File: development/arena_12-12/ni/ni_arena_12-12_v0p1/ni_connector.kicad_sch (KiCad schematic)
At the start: 29 parts, among them J2 NI_TE_68pos

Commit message: Worked on fabrication setup for NI 12-12 arena.
Added part numbers, datasheets, etc. to symbol table.
Deleted old productions files.
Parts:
- J2: Digikey PN (none) -> A123166-ND; LCSC Part # (none) -> TODO; MPN (none) -> 5174339-5
- R1, R10, R11, R12, R13, R14, R15, R16, R17, R18, R19, R2, R20, R21, R22, R23, R24, R25, R26, R27, R28, R3, R4, R5, R6, R7, R8, R9: Digikey PN (none) -> (none); LCSC Part # (none) -> C25105; MPN (none) -> 0402WGF330JTCE

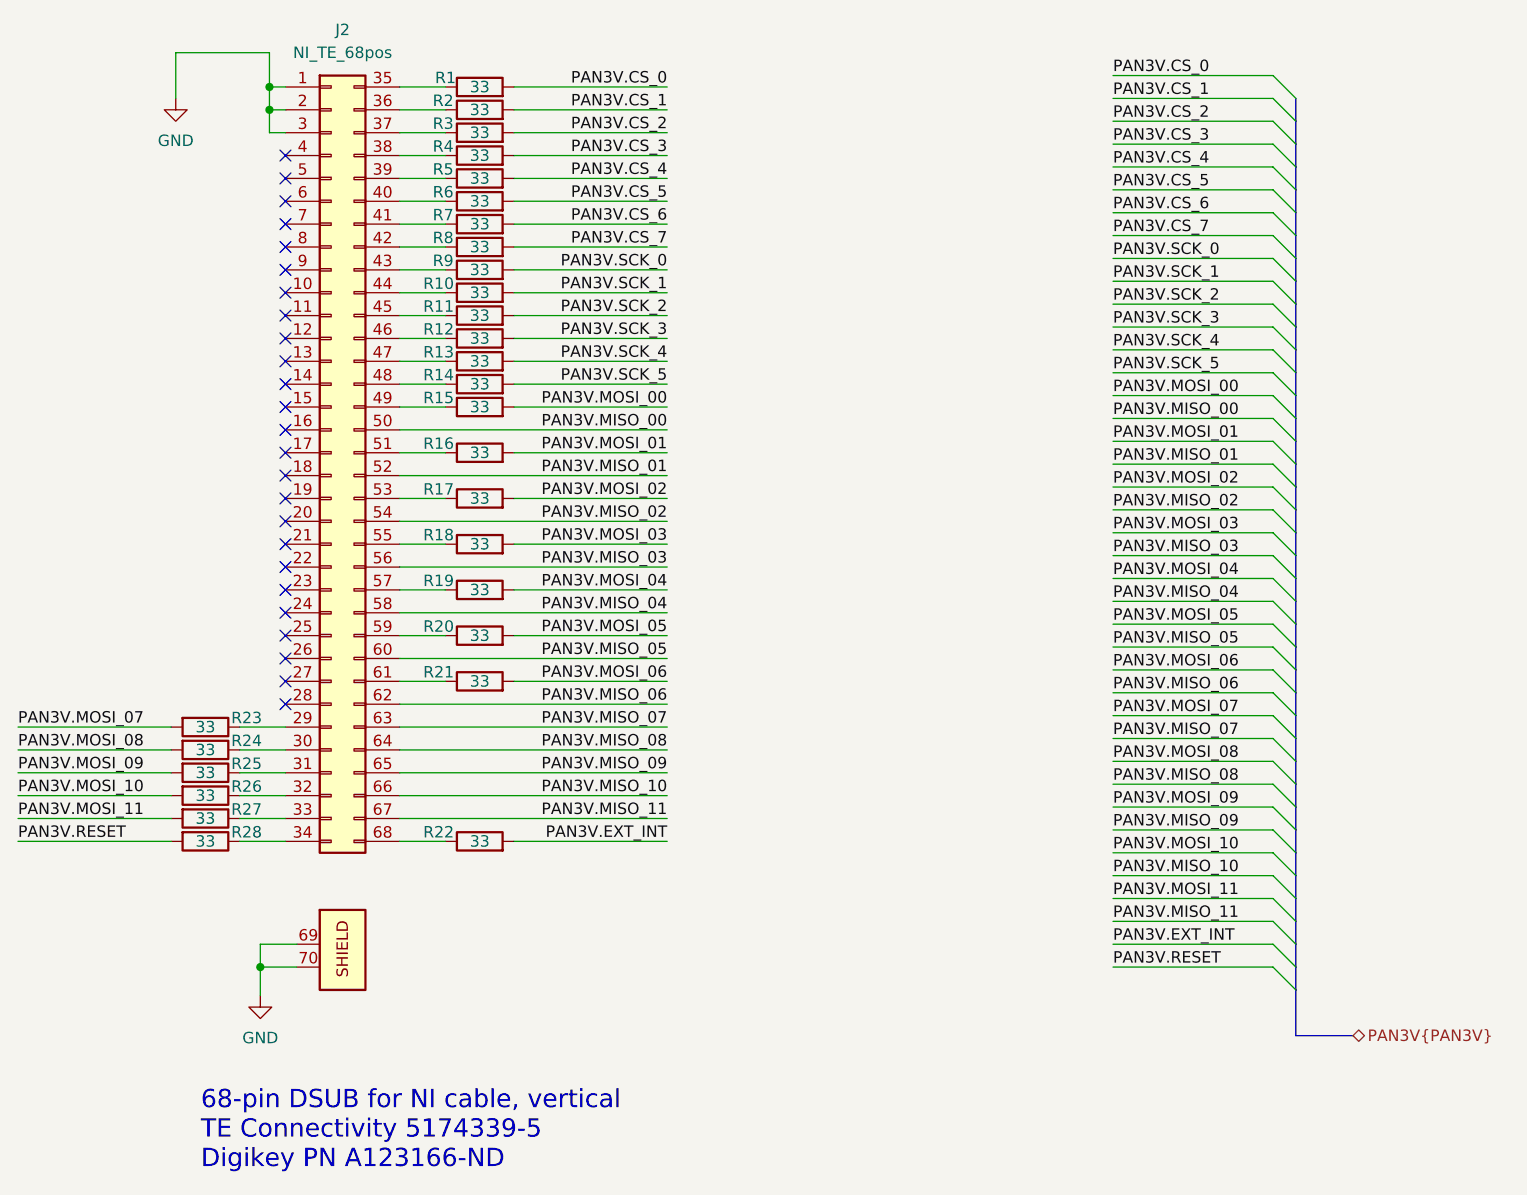
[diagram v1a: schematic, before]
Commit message: Updated pcb from schematic so LCSC Part # appear in BOM file.
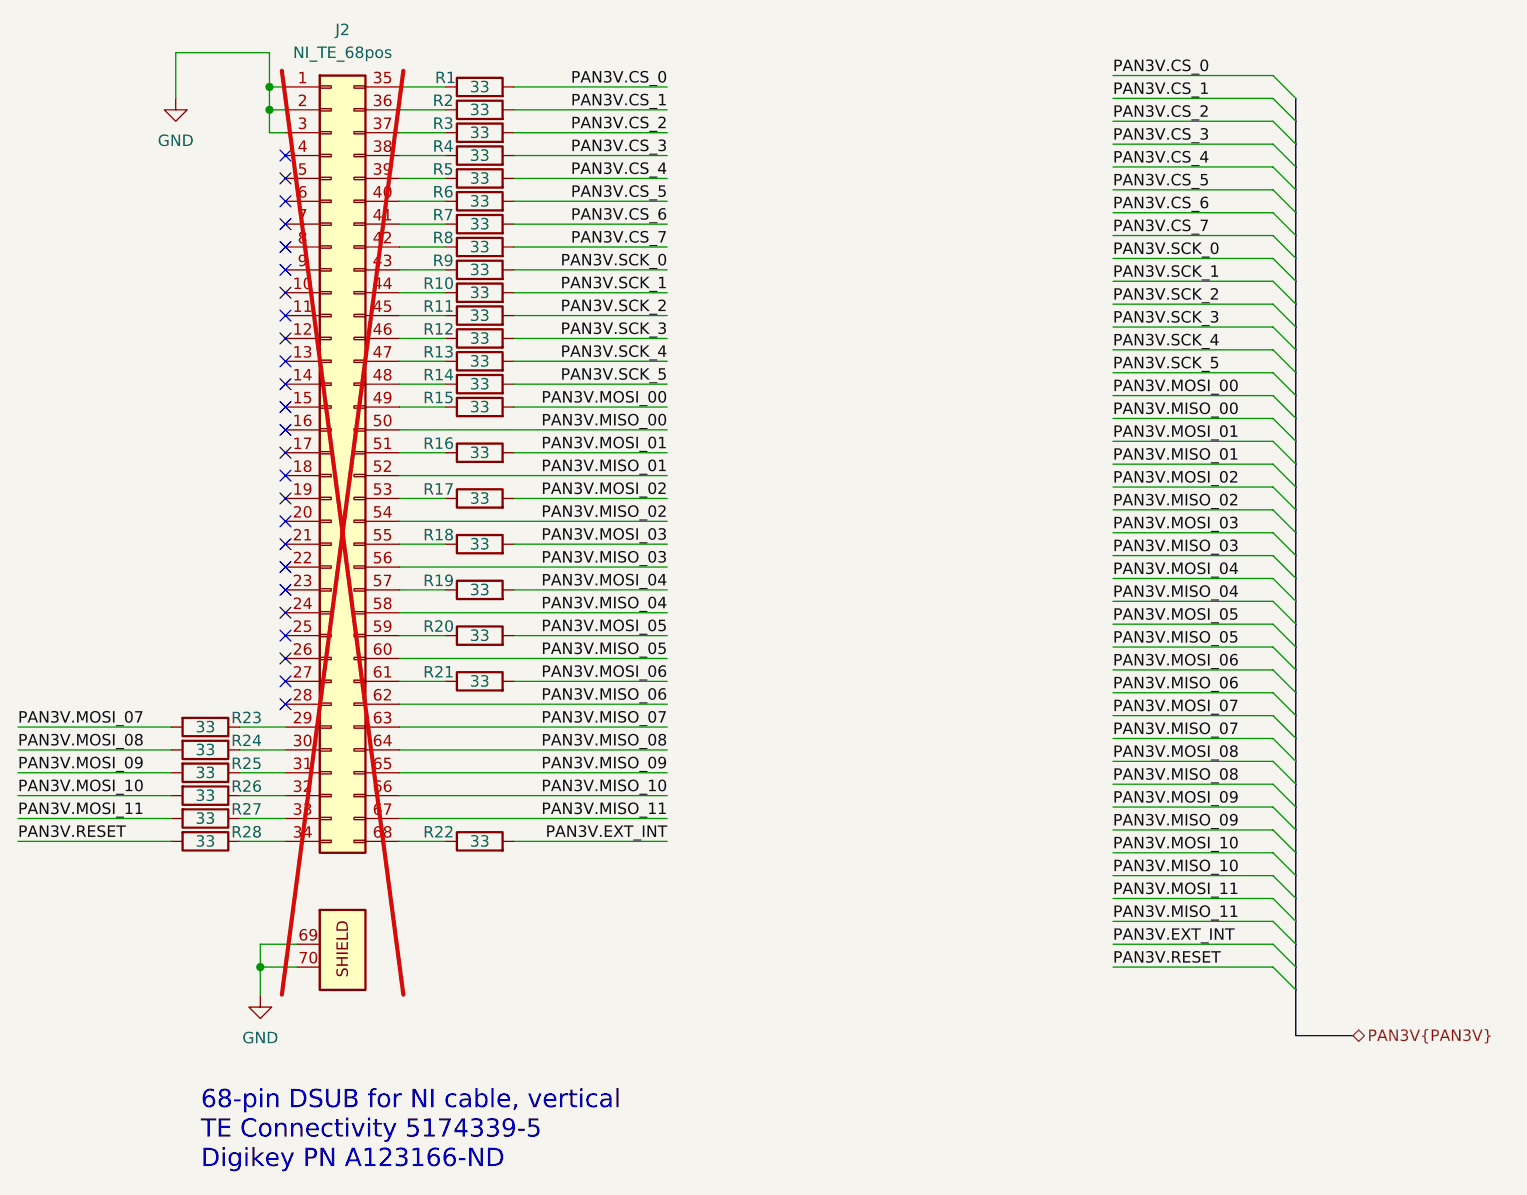
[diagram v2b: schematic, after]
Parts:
- J2: LCSC Part # TODO -> (none); now not fitted
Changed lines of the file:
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@@
 		(in_bom yes)
 		(on_board yes)
-		(dnp no)
+		(dnp yes)
 		(fields_autoplaced yes)
 		(property "Reference" "J2"
@@
 			)
 		)
-		(property "LCSC Part #" "TODO"
+		(property "LCSC Part #" ""
 			(at 93.472 67.31 0)
 			(effects

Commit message: Finished preliminary production setup for NI 12-12 arena with schmitt buffers.
Note,  rotation offsets may still adjusting (for 74LVC2G17's and Q1)
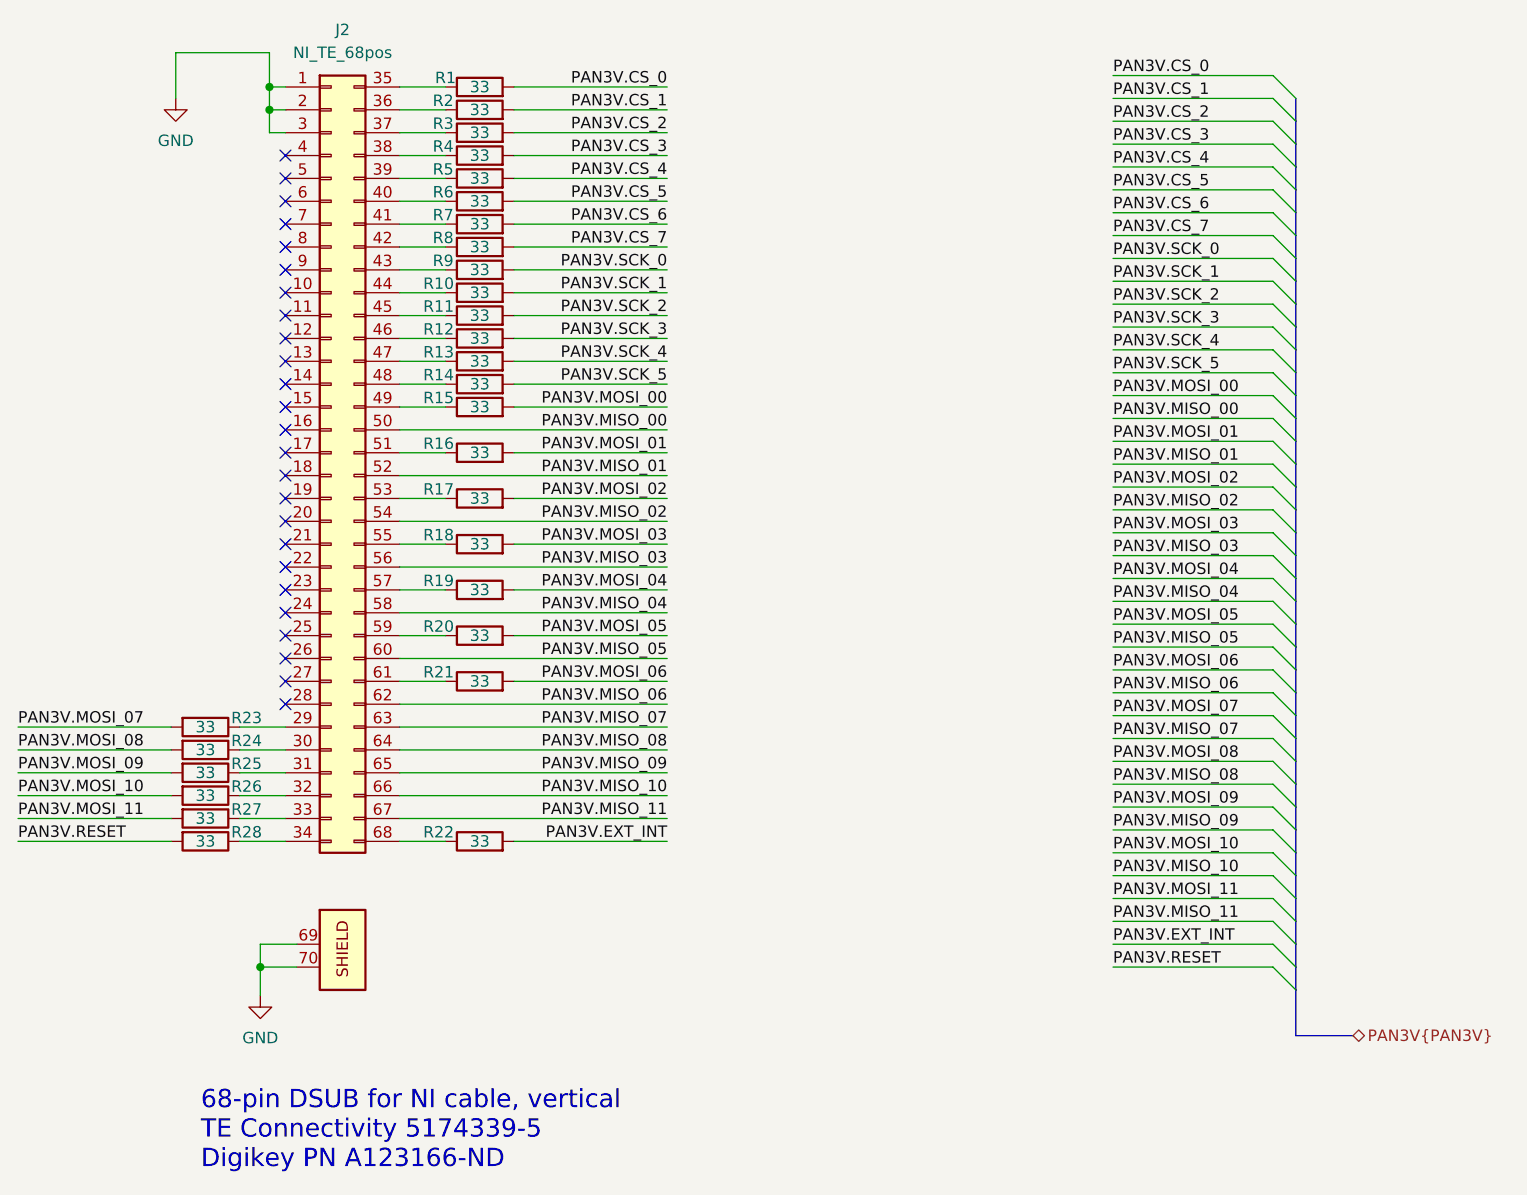
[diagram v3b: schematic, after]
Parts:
- J2: now fitted
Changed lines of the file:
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@@
 		(in_bom yes)
 		(on_board yes)
-		(dnp yes)
+		(dnp no)
 		(fields_autoplaced yes)
 		(property "Reference" "J2"

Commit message: project cleanup prior to ordering
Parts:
- J2: LCSC Part # (none) -> C5172587
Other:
- company: (none) -> IORodeo for Reiserlab @ Janelia
- title: (none) -> 12-12 NI G4.1 Arena Modular LED Display
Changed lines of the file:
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@@
 	(generator_version "9.0")
 	(paper "A4")
+	(title_block
+		(title "12-12 NI G4.1 Arena Modular LED Display")
+		(date "2025-04-21")
+		(rev "v0.3.4")
+		(company "IORodeo for Reiserlab @ Janelia")
+	)
 	(bus_alias "PAN3V"
 		(members "CS_0" "CS_1" "CS_2" "CS_3" "CS_4" "CS_5" "CS_6" "CS_7" "SCK_0"
@@
 			)
 		)
-		(property "LCSC Part #" ""
+		(property "LCSC Part #" "C5172587"
 			(at 93.472 67.31 0)
 			(effects

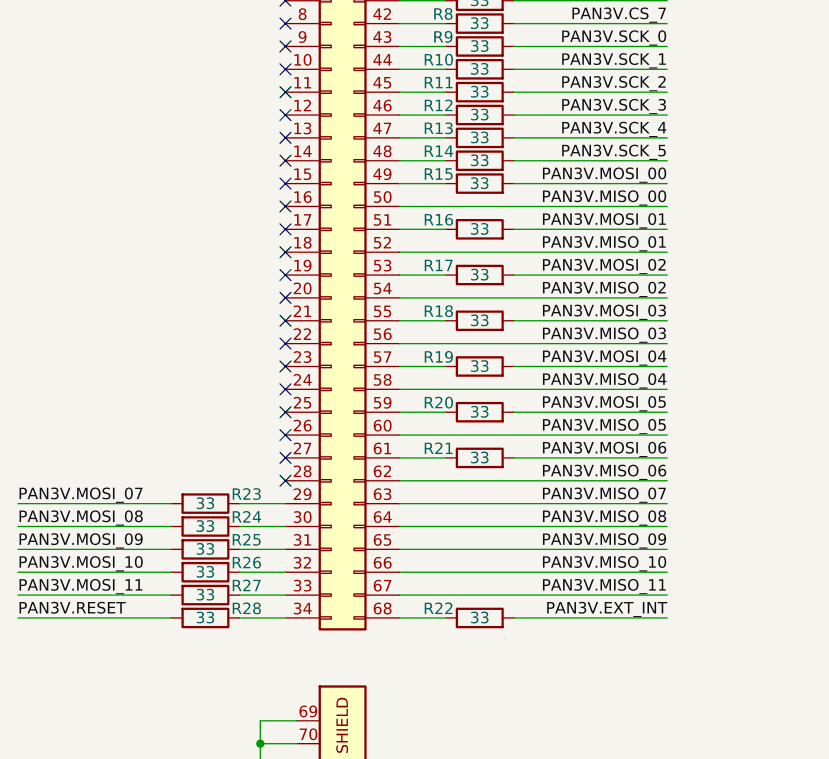
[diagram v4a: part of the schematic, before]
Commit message: reroute arena to imitate G4
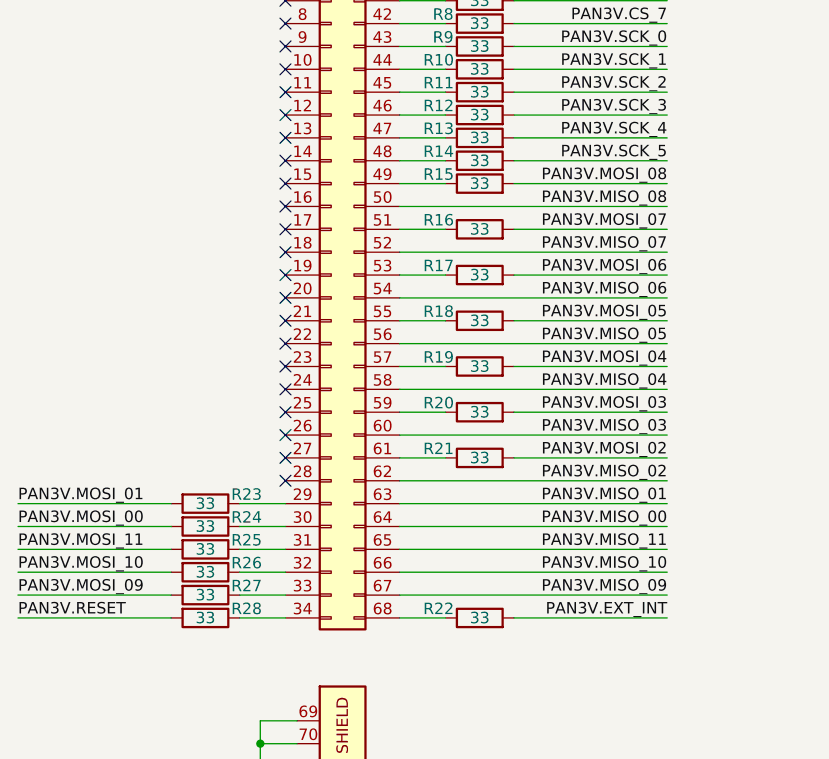
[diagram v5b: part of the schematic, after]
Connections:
- net PAN3V.MISO_00: now also J2.64 (Pin_64); no longer J2.50 (Pin_50)
- net PAN3V.MISO_01: now also J2.63 (Pin_63); no longer J2.52 (Pin_52)
- net PAN3V.MISO_02: now also J2.62 (Pin_62); no longer J2.54 (Pin_54)
- net PAN3V.MISO_03: now also J2.60 (Pin_60); no longer J2.56 (Pin_56)
- net PAN3V.MISO_05: now also J2.56 (Pin_56); no longer J2.60 (Pin_60)
- net PAN3V.MISO_06: now also J2.54 (Pin_54); no longer J2.62 (Pin_62)
- net PAN3V.MISO_07: now also J2.52 (Pin_52); no longer J2.63 (Pin_63)
- net PAN3V.MISO_08: now also J2.50 (Pin_50); no longer J2.64 (Pin_64)
- net PAN3V.MISO_09: now also J2.67 (Pin_67); no longer J2.65 (Pin_65)
- net PAN3V.MISO_11: now also J2.65 (Pin_65); no longer J2.67 (Pin_67)
- net PAN3V.MOSI_00: now also R24.2; no longer R15.2
- net PAN3V.MOSI_01: now also R23.2; no longer R16.2
- net PAN3V.MOSI_02: now also R21.2; no longer R17.2
- net PAN3V.MOSI_03: now also R20.2; no longer R18.2
- net PAN3V.MOSI_05: now also R18.2; no longer R20.2
- net PAN3V.MOSI_06: now also R17.2; no longer R21.2
- net PAN3V.MOSI_07: now also R16.2; no longer R23.2
- net PAN3V.MOSI_08: now also R15.2; no longer R24.2
- net PAN3V.MOSI_09: now also R27.2; no longer R25.2
- net PAN3V.MOSI_11: now also R25.2; no longer R27.2
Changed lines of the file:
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@@
 	(title_block
 		(title "12-12 NI G4.1 Arena Modular LED Display")
-		(date "2025-04-21")
-		(rev "v0.3.4")
+		(date "2025-08-06")
+		(rev "v0.4")
 		(company "IORodeo for Reiserlab @ Janelia")
 	)
@@
 		)
 	)
-	(label "PAN3V.MOSI_07"
+	(label "PAN3V.MOSI_01"
 		(at 58.674 97.79 0)
 		(effects
@@
 		)
 	)
-	(label "PAN3V.MOSI_01"
+	(label "PAN3V.MOSI_07"
 		(at 130.81 67.31 180)
 		(effects
@@
 		)
 	)
-	(label "PAN3V.MOSI_03"
+	(label "PAN3V.MOSI_05"
 		(at 130.81 77.47 180)
 		(effects
@@
 		)
 	)
-	(label "PAN3V.MOSI_05"
+	(label "PAN3V.MOSI_03"
 		(at 130.81 87.63 180)
 		(effects
@@
 		)
 	)
-	(label "PAN3V.MOSI_08"
+	(label "PAN3V.MOSI_00"
 		(at 58.674 100.33 0)
 		(effects
@@
 		)
 	)
-	(label "PAN3V.MISO_03"
+	(label "PAN3V.MISO_05"
 		(at 130.81 80.01 180)
 		(effects
@@
 		)
 	)
-	(label "PAN3V.MOSI_00"
+	(label "PAN3V.MOSI_08"
 		(at 130.81 62.23 180)
 		(effects
@@
 		)
 	)
-	(label "PAN3V.MOSI_11"
+	(label "PAN3V.MOSI_09"
 		(at 58.674 107.95 0)
 		(effects
@@
 		)
 	)
-	(label "PAN3V.MISO_01"
+	(label "PAN3V.MISO_07"
 		(at 130.81 69.85 180)
 		(effects
@@
 		)
 	)
-	(label "PAN3V.MISO_11"
+	(label "PAN3V.MISO_09"
 		(at 130.81 107.95 180)
 		(effects
@@
 		)
 	)
-	(label "PAN3V.MOSI_06"
+	(label "PAN3V.MOSI_02"
 		(at 130.81 92.71 180)
 		(effects
@@
 		)
 	)
-	(label "PAN3V.MISO_09"
+	(label "PAN3V.MISO_11"
 		(at 130.81 102.87 180)
 		(effects
@@
 		)
 	)
-	(label "PAN3V.MISO_05"
+	(label "PAN3V.MISO_03"
 		(at 130.81 90.17 180)
 		(effects
@@
 		)
 	)
-	(label "PAN3V.MOSI_09"
+	(label "PAN3V.MOSI_11"
 		(at 58.674 102.87 0)
 		(effects
@@
 		)
 	)
+	(label "PAN3V.MISO_02"
+		(at 130.81 95.25 180)
+		(effects
+			(font
+				(size 1.27 1.27)
+			)
+			(justify right bottom)
+		)
+	)
 	(label "PAN3V.MISO_06"
-		(at 130.81 95.25 180)
-		(effects
-			(font
-				(size 1.27 1.27)
-			)
-			(justify right bottom)
-		)
-	)
-	(label "PAN3V.MISO_02"
 		(at 130.81 74.93 180)
 		(effects
@@
 		)
 	)
-	(label "PAN3V.MISO_07"
+	(label "PAN3V.MISO_01"
 		(at 130.81 97.79 180)
 		(effects
@@
 		)
 	)
-	(label "PAN3V.MISO_00"
+	(label "PAN3V.MISO_08"
 		(at 130.81 64.77 180)
 		(effects
@@
 		)
 	)
-	(label "PAN3V.MOSI_02"
+	(label "PAN3V.MOSI_06"
 		(at 130.81 72.39 180)
 		(effects
@@
 		)
 	)
-	(label "PAN3V.MISO_08"
+	(label "PAN3V.MISO_00"
 		(at 130.81 100.33 180)
 		(effects
